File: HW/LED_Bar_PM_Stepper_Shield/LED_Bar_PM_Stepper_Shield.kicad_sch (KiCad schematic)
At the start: 2 parts

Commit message: Done something.
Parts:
- removed D1: LED_BAGR, symbol Device:LED_BAGR
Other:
- added sheet Untitled Sheet (ULN_LED_BAR_2x_Steppers.kicad_sch)
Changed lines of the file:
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@@
-	)
-	(symbol
-		(lib_id "Device:LED_BAGR")
-		(at 214.63 67.31 0)
-		(unit 1)
-		(exclude_from_sim no)
-		(in_bom yes)
-		(on_board yes)
-		(dnp no)
-		(fields_autoplaced yes)
-		(property "Reference" "D1"
-			(at 214.63 53.34 0)
-			(effects
-				(font
-					(size 1.27 1.27)
-				)
-			)
-		)
-		(property "Value" "LED_BAGR"
-			(at 214.63 55.88 0)
-			(effects
-				(font
-					(size 1.27 1.27)
-				)
-			)
-		)
-		(property "Footprint" ""
-			(at 214.63 68.58 0)
-			(effects
-				(font
-					(size 1.27 1.27)
-				)
-				(hide yes)
-			)
-		)
-		(property "Datasheet" "~"
-			(at 214.63 68.58 0)
-			(effects
-				(font
-					(size 1.27 1.27)
-				)
-				(hide yes)
-			)
-		)
-		(property "Description" "RGB LED, blue/anode/green/red"
-			(at 214.63 67.31 0)
-			(effects
-				(font
-					(size 1.27 1.27)
-				)
-				(hide yes)
-			)
-		)
-		(pin "3"
-		)
-		(pin "2"
-		)
-		(pin "1"
-		)
-		(pin "4"
-		)
-		(instances
-			(project ""
-				(path "/f032f0f5-bc12-4ceb-9247-9ea9649022af"
-					(reference "D1")
-					(unit 1)
-				)
-			)
-		)
 	)
 	(symbol
@@
 				)
 			)
+		)
+	)
+	(sheet
+		(at 175.26 53.34)
+		(size 30.48 35.56)
+		(fields_autoplaced yes)
+		(stroke
+			(width 0.1524)
+			(type solid)
+		)
+		(fill
+			(color 0 0 0 0.0000)
+		)
+		(property "Sheetname" "Untitled Sheet"
+			(at 175.26 52.6284 0)
+			(effects
+				(font
+					(size 1.27 1.27)
+				)
+				(justify left bottom)
+			)
+		)
+		(property "Sheetfile" "ULN_LED_BAR_2x_Steppers.kicad_sch"
+			(at 175.26 89.4846 0)
+			(effects
+				(font
+					(size 1.27 1.27)
+				)
+				(justify left top)
+			)
+		)
+		(instances
+			(project "LED_Bar_PM_Stepper_Shield"
+				(path "/f032f0f5-bc12-4ceb-9247-9ea9649022af"
+					(page "2")
+				)
+			)

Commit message: Done PCB.
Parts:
- added H1, H2, H3, H4: M3, MountingHole:MountingHole_3.2mm_M3, symbol Mechanical:MountingHole
- added J5, J6: 1x6 2.54mm female, pin2 filled, Connector_PinHeader_2.54mm:PinHeader_1x06_P2.54mm_Vertical, symbol Connector:Conn_01x06_Socket
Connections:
- net +5V: now also J5.5 (Pin_5), J6.5 (Pin_5)
- net GND: now also A1.29 (GND), J5.1 (Pin_1), J6.1 (Pin_1)
- net b0/B1: now reaches A1.1 (D1/TX)
- net DA0: now reaches A1.16 (D13)
- net DA0: now also J5.4 (Pin_4)
- net b0/B0: now reaches A1.2 (D0/RX)
- net A0: now reaches A1.25 (A6)
- net A0: now also J5.3 (Pin_3)
- net A1: now reaches A1.26 (A7)
- net A1: now also J6.3 (Pin_3)
- net A0__AIN2 renamed L0
- net A1__D0 renamed L1
- net A2__D1 renamed L2
- net A3__D2 renamed L3
- net A4__D3 renamed DB1
- net DB1: now also J6.6 (Pin_6)
- net A5__D4 renamed DA1
- net DA1: now also J6.4 (Pin_4)
- net D10__AIN0 renamed b1/B2
- net D11__AIN4 renamed b1/B3
- net D12__AIN3 renamed DB0
- net DB0: now also J5.6 (Pin_6)
- net D2__D5 renamed b0/B2
- net D3__D6 renamed b0/B3
- net D4__D7 renamed b0/B4
- net D5__D8 renamed b0/B5
- net D6__D9 renamed b0/B6
- net D7__D10 renamed b0/B7
- net D8__D11 renamed b1/B0
- net D9__D12 renamed b1/B1
- no-connect marks 8 -> 7
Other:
- sheet Untitled Sheet renamed b0
- added sheet b1 (Bank.kicad_sch)
- sheet b0: file ULN_LED_BAR_2x_Steppers.kicad_sch -> Bank.kicad_sch
- sheet b0 ports: added B0, B1, B2, B3, B4, B5, B6, B7; removed none
- note added: "GND FILLED A DA VCC DB"
- note added: "If you want to use Serial.print() i.e. UART Tx, you cannot use bank0.channel0 PM stepper."
- note removed: "<Arduino pin name>__<MAX1000 pin name>"
- note removed: "Pull out pin from connector for every you do not use A1: 1 2 3 17 18 25 26 28 29 30 J1: 8 9 10 12 13 J2: 1 7 8"

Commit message: Small corrections.
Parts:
- added J7, J8: Extension of Ard Nano, filled, Connector_PinSocket_2.54mm:PinSocket_1x01_P2.54mm_Vertical, symbol Connector:Conn_01x01_Socket
- A1: Comment (none) -> pin 3, RST is filled
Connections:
- net +5V: now also J7.1 (Pin_1), J8.1 (Pin_1)
- net GND: no longer A1.4 (GND)
- no-connect marks 7 -> 8

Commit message: PCB corrected.
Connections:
- net +5V: no longer J7.1 (Pin_1), J8.1 (Pin_1)
- net GND: now also J7.1 (Pin_1), J8.1 (Pin_1)
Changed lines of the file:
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@@
+	)
+	(symbol
+		(lib_id "power:GND")
+		(at 99.06 113.03 270)
+		(unit 1)
+		(exclude_from_sim no)
+		(in_bom yes)
+		(on_board yes)
+		(dnp no)
+		(fields_autoplaced yes)
+		(property "Reference" "#PWR14"
+			(at 92.71 113.03 0)
+			(effects
+				(font
+					(size 1.27 1.27)
+				)
+				(hide yes)
+			)
+		)
+		(property "Value" "GND"
+			(at 95.25 113.0299 90)
+			(effects
+				(font
+					(size 1.27 1.27)
+				)
+				(justify right)
+			)
+		)
+		(property "Footprint" ""
+			(at 99.06 113.03 0)
+			(effects
+				(font
+					(size 1.27 1.27)
+				)
+				(hide yes)
+			)
+		)
+		(property "Datasheet" ""
+			(at 99.06 113.03 0)
+			(effects
+				(font
+					(size 1.27 1.27)
+				)
+				(hide yes)
+			)
+		)
+		(property "Description" "Power symbol creates a global label with name \"GND\" , ground"
+			(at 99.06 113.03 0)
+			(effects
+				(font
+					(size 1.27 1.27)
+				)
+				(hide yes)
+			)
+		)
+		(pin "1"
+		)
+		(instances
+			(project "LED_Bar_PM_Stepper_Shield"
+				(path "/f032f0f5-bc12-4ceb-9247-9ea9649022af"
+					(reference "#PWR14")
+					(unit 1)
+				)
+			)
+		)
 	)
 	(symbol
@@
 	)
 	(symbol
+		(lib_id "power:GND")
+		(at 99.06 106.68 270)
+		(unit 1)
+		(exclude_from_sim no)
+		(in_bom yes)
+		(on_board yes)
+		(dnp no)
+		(fields_autoplaced yes)
+		(property "Reference" "#PWR13"
+			(at 92.71 106.68 0)
+			(effects
+				(font
+					(size 1.27 1.27)
+				)
+				(hide yes)
+			)
+		)
+		(property "Value" "GND"
+			(at 95.25 106.6799 90)
+			(effects
+				(font
+					(size 1.27 1.27)
+				)
+				(justify right)
+			)
+		)
+		(property "Footprint" ""
+			(at 99.06 106.68 0)
+			(effects
+				(font
+					(size 1.27 1.27)
+				)
+				(hide yes)
+			)
+		)
+		(property "Datasheet" ""
+			(at 99.06 106.68 0)
+			(effects
+				(font
+					(size 1.27 1.27)
+				)
+				(hide yes)
+			)
+		)
+		(property "Description" "Power symbol creates a global label with name \"GND\" , ground"
+			(at 99.06 106.68 0)
+			(effects
+				(font
+					(size 1.27 1.27)
+				)
+				(hide yes)
+			)
+		)
+		(pin "1"
+		)
+		(instances
+			(project ""
+				(path "/f032f0f5-bc12-4ceb-9247-9ea9649022af"
+					(reference "#PWR13")
+					(unit 1)
+				)
+			)
+		)
+	)
+	(symbol
 		(lib_id "Connector:Conn_01x01_Socket")
 		(at 106.68 113.03 0)
@@
 				(path "/f032f0f5-bc12-4ceb-9247-9ea9649022af"
 					(reference "J8")
-					(unit 1)
-				)
-			)
-		)
-	)
-	(symbol
-		(lib_id "power:+5V")
-		(at 99.06 106.68 90)
-		(unit 1)
-		(exclude_from_sim no)
-		(in_bom yes)
-		(on_board yes)
-		(dnp no)
-		(fields_autoplaced yes)
-		(property "Reference" "#PWR13"
-			(at 102.87 106.68 0)
-			(effects
-				(font
-					(size 1.27 1.27)
-				)
-				(hide yes)
-			)
-		)
-		(property "Value" "+5V"
-			(at 95.25 106.6799 90)
-			(effects
-				(font
-					(size 1.27 1.27)
-				)
-				(justify left)
-			)
-		)
-		(property "Footprint" ""
-			(at 99.06 106.68 0)
-			(effects
-				(font
-					(size 1.27 1.27)
-				)
-				(hide yes)
-			)
-		)
-		(property "Datasheet" ""
-			(at 99.06 106.68 0)
-			(effects
-				(font
-					(size 1.27 1.27)
-				)
-				(hide yes)
-			)
-		)
-		(property "Description" "Power symbol creates a global label with name \"+5V\""
-			(at 99.06 106.68 0)
-			(effects
-				(font
-					(size 1.27 1.27)
-				)
-				(hide yes)
-			)
-		)
-		(pin "1"
-		)
-		(instances
-			(project ""
-				(path "/f032f0f5-bc12-4ceb-9247-9ea9649022af"
-					(reference "#PWR13")
 					(unit 1)
 				)
@@
 					(unit 1)
 				)
-			)
-		)
-	)
-	(symbol
-		(lib_id "power:+5V")
-		(at 99.06 113.03 90)
-		(unit 1)
-		(exclude_from_sim no)
-		(in_bom yes)
-		(on_board yes)
-		(dnp no)
-		(fields_autoplaced yes)
-		(property "Reference" "#PWR14"
-			(at 102.87 113.03 0)
-			(effects
-				(font
-					(size 1.27 1.27)
-				)
-				(hide yes)
-			)
-		)
-		(property "Value" "+5V"
-			(at 95.25 113.0299 90)
-			(effects
-				(font
-					(size 1.27 1.27)
-				)
-				(justify left)
-			)
-		)
-		(property "Footprint" ""
-			(at 99.06 113.03 0)
-			(effects
-				(font
-					(size 1.27 1.27)
-				)
-				(hide yes)
-			)
-		)
-		(property "Datasheet" ""
-			(at 99.06 113.03 0)
-			(effects
-				(font
-					(size 1.27 1.27)
-				)
-				(hide yes)
-			)
-		)
-		(property "Description" "Power symbol creates a global label with name \"+5V\""
-			(at 99.06 113.03 0)
-			(effects
-				(font
-					(size 1.27 1.27)
-				)
-				(hide yes)
-			)
-		)
-		(pin "1"
-		)
-		(instances
-			(project "LED_Bar_PM_Stepper_Shield"
-				(path "/f032f0f5-bc12-4ceb-9247-9ea9649022af"
-					(reference "#PWR14")
-					(unit 1)
-				)

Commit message: Resistors.
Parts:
- added R1, R2, R3, R4: 10k, For_Rasterboard:R_Axial_DIN0207_L6.3mm_D2.5mm_Pinf_Horizontal, symbol Device:R
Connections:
- net DA0: now also R3.2
- net DA1: now also R1.2
- net DB0: now also R4.2
- net DB1: now also R2.2
- net GND: now also R1.1, R2.1, R3.1, R4.1
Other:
- moved on the sheet: J5, J6

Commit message: Correction.
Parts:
- added JP1: Jumper_2_Open, Connector_PinHeader_2.54mm:PinHeader_1x02_P2.54mm_Vertical, symbol Jumper:Jumper_2_Open
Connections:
- net +5V: now also JP1.2 (B); no longer A1.27 (+5V)
- new net: A1.27 (+5V), JP1.1 (A)
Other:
- note added: "TODO 5V jack, maybe protection, try zener"
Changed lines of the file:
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@@
+	(wire
+		(pts
+			(xy 121.92 30.48) (xy 132.08 30.48)
+		)
+		(stroke
+			(width 0)
+			(type default)
+		)
+	)
 	(wire
 		(pts
@@
 	(wire
 		(pts
+			(xy 142.24 30.48) (xy 152.4 30.48)
+		)
+		(stroke
+			(width 0)
+			(type default)
+		)
+	)
+	(wire
+		(pts
 			(xy 59.69 53.34) (xy 104.14 53.34)
 		)
@@
 			)
 			(justify left)
+		)
+	)
+	(text "TODO 5V jack, maybe protection, try zener"
+		(exclude_from_sim no)
+		(at 214.884 28.194 0)
+		(effects
+			(font
+				(size 1.27 1.27)
+			)
 		)
 	)
@@
 	)
 	(symbol
+		(lib_id "Jumper:Jumper_2_Open")
+		(at 137.16 30.48 0)
+		(unit 1)
+		(exclude_from_sim yes)
+		(in_bom yes)
+		(on_board yes)
+		(dnp no)
+		(fields_autoplaced yes)
+		(property "Reference" "JP1"
+			(at 137.16 24.13 0)
+			(effects
+				(font
+					(size 1.27 1.27)
+				)
+			)
+		)
+		(property "Value" "Jumper_2_Open"
+			(at 137.16 26.67 0)
+			(effects
+				(font
+					(size 1.27 1.27)
+				)
+			)
+		)
+		(property "Footprint" "Connector_PinHeader_2.54mm:PinHeader_1x02_P2.54mm_Vertical"
+			(at 137.16 30.48 0)
+			(effects
+				(font
+					(size 1.27 1.27)
+				)
+				(hide yes)
+			)
+		)
+		(property "Datasheet" "~"
+			(at 137.16 30.48 0)
+			(effects
+				(font
+					(size 1.27 1.27)
+				)
+				(hide yes)
+			)
+		)
+		(property "Description" "Jumper, 2-pole, open"
+			(at 137.16 30.48 0)
+			(effects
+				(font
+					(size 1.27 1.27)
+				)
+				(hide yes)
+			)
+		)
+		(pin "2"
+		)
+		(pin "1"
+		)
+		(instances
+			(project ""
+				(path "/f032f0f5-bc12-4ceb-9247-9ea9649022af"
+					(reference "JP1")
+					(unit 1)
+				)
+			)
+		)
+	)
+	(symbol
 		(lib_id "power:GND")
 		(at 160.02 83.82 270)
@@
 	(symbol
 		(lib_id "LPRS1_MAX1000_Shield-rescue:+5V-power")
-		(at 121.92 30.48 0)
+		(at 152.4 30.48 0)
 		(unit 1)
 		(exclude_from_sim no)
@@
 		(dnp no)
 		(property "Reference" "#PWR102"
-			(at 121.92 34.29 0)
+			(at 152.4 34.29 0)
 			(effects
 				(font
@@
 		)
 		(property "Value" "+5V"
-			(at 122.301 26.0858 0)
+			(at 152.781 26.0858 0)
 			(effects
 				(font
@@
 		)
 		(property "Footprint" ""
-			(at 121.92 30.48 0)
+			(at 152.4 30.48 0)
 			(effects
 				(font
@@
 		)
 		(property "Datasheet" ""
-			(at 121.92 30.48 0)
+			(at 152.4 30.48 0)
 			(effects
 				(font
@@
 		)
 		(property "Description" ""
-			(at 121.92 30.48 0)
-			(effects
-				(font
+			(at 152.4 30.48 0)
+			(effects
+				(font

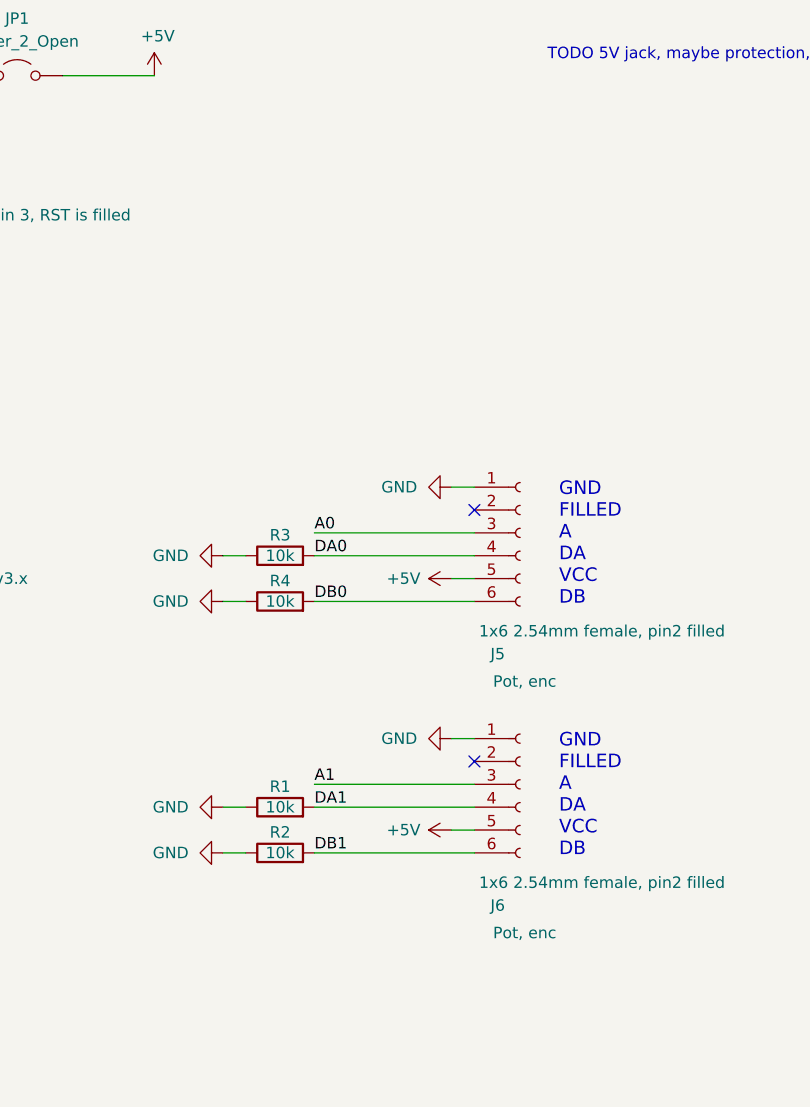
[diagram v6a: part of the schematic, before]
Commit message: Enc from robot.
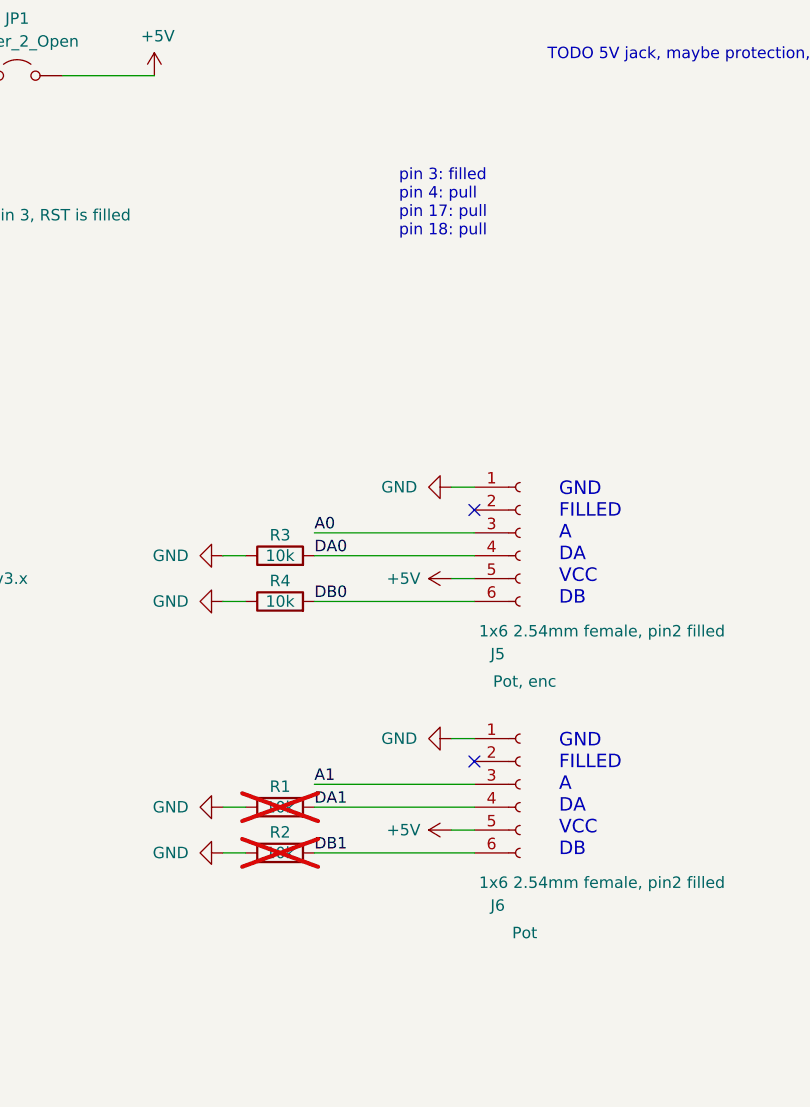
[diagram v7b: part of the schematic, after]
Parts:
- J6: Comment Pot, enc -> Pot
- R1, R2: now not fitted
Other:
- note added: "pin 3: filled pin 4: pull pin 17: pull pin 18: pull"
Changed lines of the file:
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@@
+		)
+	)
+	(text "pin 3: filled\npin 4: pull\npin 17: pull\npin 18: pull"
+		(exclude_from_sim no)
+		(at 179.578 44.704 0)
+		(effects
+			(font
+				(size 1.27 1.27)
+			)
+			(justify left)
 		)
 	)
@@
 		(in_bom yes)
 		(on_board yes)
-		(dnp no)
+		(dnp yes)
 		(property "Reference" "R2"
 			(at 166.37 114.554 90)
@@
 		(in_bom yes)
 		(on_board yes)
-		(dnp no)
+		(dnp yes)
 		(property "Reference" "R1"
 			(at 166.37 109.474 90)
@@
 			)
 		)
-		(property "Comment" "Pot, enc"
+		(property "Comment" "Pot"
 			(at 193.548 125.73 0)
 			(effects

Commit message: A
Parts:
- J6: Comment Pot -> Pot, pot enc from robot hand
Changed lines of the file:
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@@
 			)
 		)
-		(property "Comment" "Pot"
+		(property "Comment" "Pot, pot enc from robot hand"
 			(at 193.548 125.73 0)
 			(effects
